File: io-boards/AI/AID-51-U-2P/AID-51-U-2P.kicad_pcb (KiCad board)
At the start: 2 copper layers, 50 x 33 mm, 24 parts, among them J1 AIP_Conn_01x12_Pin, J2 Conn_01x03_Pin, J3 Conn_01x02_Socket, J4 Conn_01x03_Socket, J5 Conn_01x03_Pin, J6 Conn_01x03_Pin, U1 L78L10_SOT89

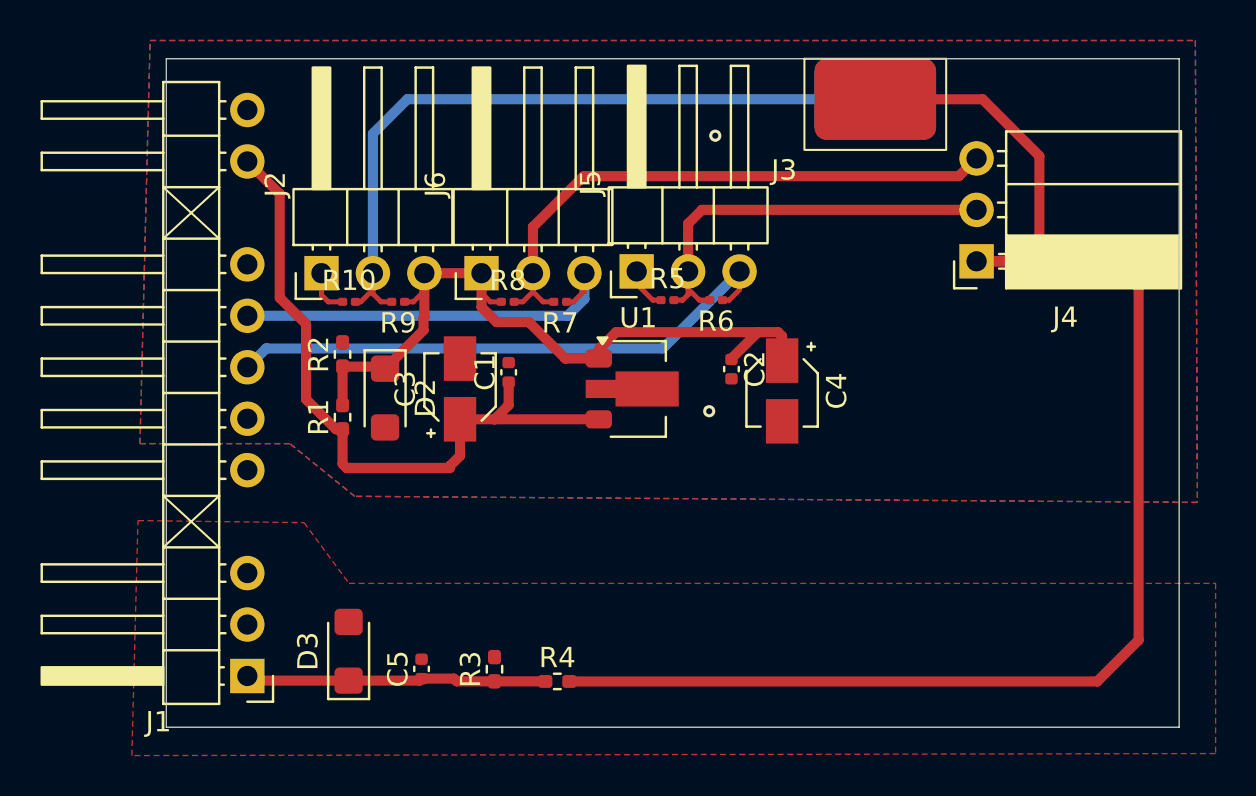
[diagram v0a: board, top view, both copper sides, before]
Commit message: Made some corrections after assembling of prototype PCBs
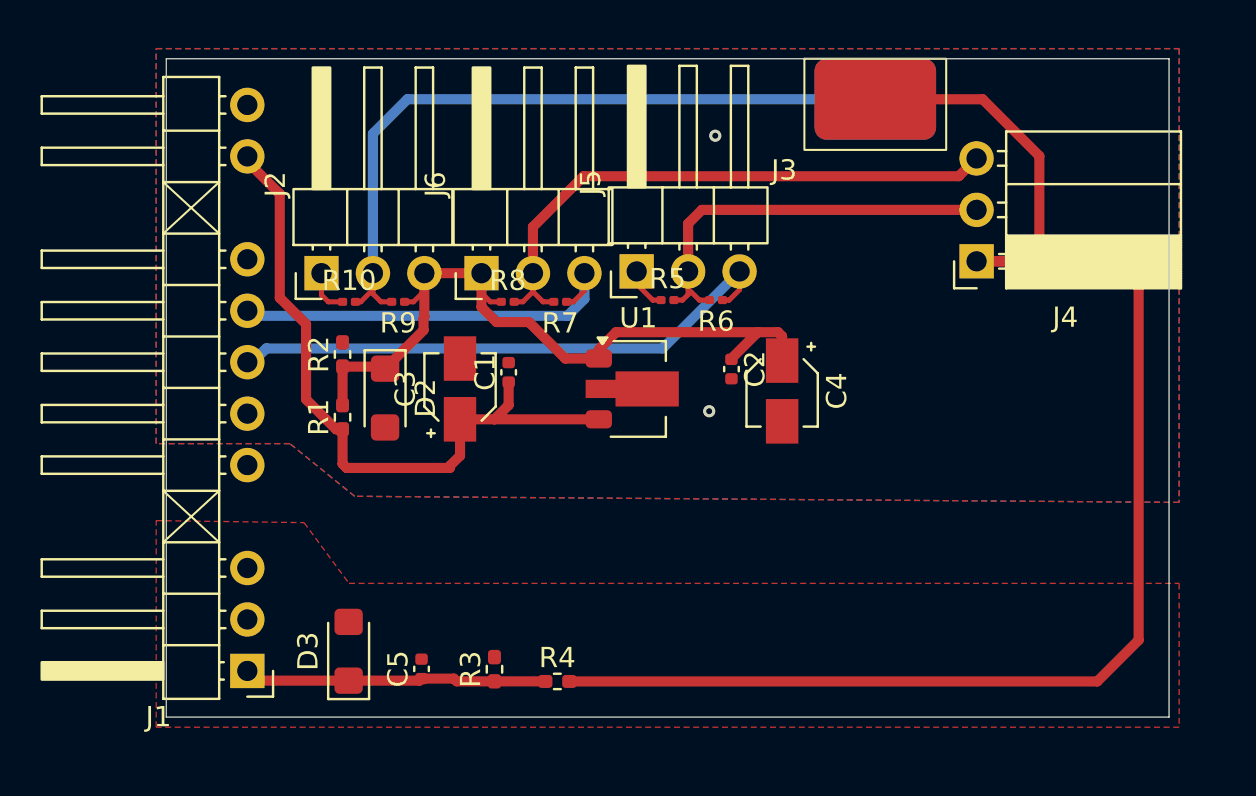
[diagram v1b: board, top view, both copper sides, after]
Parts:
- moved J1 0.25 mm to (104.0, 80.2)
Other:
- board size 50 x 33 mm -> 49.5 x 32.5 mm
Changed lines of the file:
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@@
 	(footprint "tuxmio:IO_AIP_PinHeader_1x12_P2.54mm_Horizontal"
 		(layer "F.Cu")
-		(at 104 80.47 180)
+		(at 104 80.22 180)
 		(descr "Through hole angled pin header, 1x12, 2.54mm pitch, 6mm pin length, single row")
 		(tags "Through hole angled pin header THT 1x12 2.54mm single row")
@@
 	(gr_rect
 		(start 100 50)
-		(end 150 83)
+		(end 149.5 82.5)
 		(stroke
 			(width 0.05)
@@
 	)
 	(segment
-		(start 109 80.7)
-		(end 104.23 80.7)
-		(width 0.5)
-		(layer "F.Cu")
-		(net 4)
-	)
-	(segment
 		(start 116.2 80.735)
 		(end 118.7 80.735)
@@
 	)
 	(segment
-		(start 104.23 80.7)
-		(end 104 80.47)
+		(start 109 80.7)
+		(end 104.48 80.7)
 		(width 0.5)
 		(layer "F.Cu")
@@
 	)
 	(segment
+		(start 104.48 80.7)
+		(end 104 80.22)
+		(width 0.5)
+		(layer "F.Cu")
+		(net 4)
+	)
+	(segment
+		(start 104 80.22)
+		(end 104 80.47)
+		(width 0.5)
+		(layer "F.Cu")
+		(net 4)
+	)
+	(segment
 		(start 120.1 62)
 		(end 120.64 61.46)
@@
 		(polygon
 			(pts
-				(xy 98.6 72.8) (xy 106.8 72.9) (xy 109.02 75.9) (xy 151.8 75.9) (xy 151.8 84.3) (xy 98.3 84.4)
+				(xy 99.5 72.8) (xy 106.8 72.9) (xy 109.02 75.9) (xy 150 75.9) (xy 150 83) (xy 99.5 83)
 			)
 		)
@@
 		(polygon
 			(pts
-				(xy 99.2 49.1) (xy 150.8 49.1) (xy 150.9 71.9) (xy 109.3 71.6) (xy 106.1 69) (xy 98.7 69)
+				(xy 99.5 49.5) (xy 150 49.5) (xy 150 71.9) (xy 109.3 71.6) (xy 106.1 69) (xy 99.5 69)
 			)
 		)
